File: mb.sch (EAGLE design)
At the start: 32 parts, among them J1 PJ-002BH-SMT-TR, J2 MOLEX_70543-0003MOLEX_70543-0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, J3 MOLEX_70543-0003MOLEX_70543-0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, J4 MOLEX_70543-0003MOLEX_70543-0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, J5 MOLEX_70543-0003MOLEX_70543-0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, Q1 TN0702N3-G, Q2 TN0702N3-G, Q3 TN0702N3-G, Q4 TN0702N3-G, U1 PEM1-S12-S5-S

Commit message: Finalized v1.0 prototype
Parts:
- added R12: 270, ref_lib:YAGEO-CFR-25
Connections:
- net +3.3V: no longer R10.2
- net +5V: now also R12.2
- net GND: now also R10.2, R12.1
- net WP: now also A1.A6
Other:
- moved on the sheet: R10
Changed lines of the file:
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@@
 <class number="0" name="default" width="0" drill="0">
+</class>
+<class number="1" name="POWER" width="1.524" drill="0">
 </class>
 </classes>
@@
 <part name="C3" library="860020672008_Eagle_WCAP-ATG5_rev20a" deviceset="WCAP-ATG5_5X11" device="" package3d_urn="urn:adsk.eagle:package:18308011/2" technology="_860020672001" value="0.1  µF "/>
 <part name="JP5" library="pinhead" library_urn="urn:adsk.eagle:library:325" deviceset="PINHD-1X2" device="" package3d_urn="urn:adsk.eagle:package:22435/2"/>
+<part name="R12" library="ref_lib" deviceset="YAGEO-CFR-25" device="" value="270"/>
 </parts>
 <sheets>
@@
 <attribute name="VALUE" x="-6.858" y="67.31" size="1.778" layer="96" rot="R90"/>
 </instance>
-<instance part="R10" gate="G$1" x="-17.78" y="71.12" smashed="yes" rot="R90">
-<attribute name="NAME" x="-19.2786" y="67.31" size="1.778" layer="95" rot="R90"/>
-<attribute name="VALUE" x="-14.478" y="67.31" size="1.778" layer="96" rot="R90"/>
+<instance part="R10" gate="G$1" x="-17.78" y="50.8" smashed="yes" rot="R270">
+<attribute name="NAME" x="-16.2814" y="54.61" size="1.778" layer="95" rot="R270"/>
+<attribute name="VALUE" x="-21.082" y="54.61" size="1.778" layer="96" rot="R270"/>
 </instance>
 <instance part="R11" gate="G$1" x="30.48" y="71.12" smashed="yes" rot="R90">
@@
 </busses>
 <nets>
-<net name="+12V" class="0">
+<net name="+12V" class="1">
 <segment>
 <pinref part="A1" gate="G$1" pin="VIN"/>
@@
 <pinref part="C3" gate="G$1" pin="-"/>
 <wire x1="-27.94" y1="66.04" x2="-27.94" y2="38.1" width="0.1524" layer="91"/>
-<wire x1="-27.94" y1="38.1" x2="-2.54" y2="38.1" width="0.1524" layer="91"/>
+<wire x1="-27.94" y1="38.1" x2="-17.78" y2="38.1" width="0.1524" layer="91"/>
 <junction x="-2.54" y="38.1"/>
+<pinref part="R10" gate="G$1" pin="2"/>
+<wire x1="-17.78" y1="38.1" x2="-2.54" y2="38.1" width="0.1524" layer="91"/>
+<wire x1="-17.78" y1="45.72" x2="-17.78" y2="38.1" width="0.1524" layer="91"/>
+<junction x="-17.78" y="38.1"/>
 </segment>
 </net>
@@
 <pinref part="R10" gate="G$1" pin="1"/>
 <pinref part="U$1" gate="G$1" pin="WP"/>
-<wire x1="-17.78" y1="66.04" x2="-17.78" y2="58.42" width="0.1524" layer="91"/>
+<wire x1="-17.78" y1="55.88" x2="-17.78" y2="58.42" width="0.1524" layer="91"/>
 <wire x1="-17.78" y1="58.42" x2="-2.54" y2="58.42" width="0.1524" layer="91"/>
 <label x="-17.78" y="58.42" size="1.778" layer="95"/>
+</segment>
+<segment>
+<pinref part="A1" gate="G$1" pin="A6"/>
+<wire x1="55.88" y1="38.1" x2="38.1" y2="38.1" width="0.1524" layer="91"/>
+<label x="38.1" y="38.1" size="1.778" layer="95"/>
 </segment>
 </net>
@@
 <pinref part="R9" gate="G$1" pin="2"/>
 <wire x1="-10.16" y1="76.2" x2="17.78" y2="76.2" width="0.1524" layer="91"/>
-<pinref part="R10" gate="G$1" pin="2"/>
-<wire x1="-17.78" y1="76.2" x2="-10.16" y2="76.2" width="0.1524" layer="91"/>
-<junction x="-10.16" y="76.2"/>
-<pinref part="C3" gate="G$1" pin="+"/>
-<wire x1="-27.94" y1="73.66" x2="-27.94" y2="76.2" width="0.1524" layer="91"/>
-<wire x1="-27.94" y1="76.2" x2="-17.78" y2="76.2" width="0.1524" layer="91"/>
-<junction x="-17.78" y="76.2"/>
 <label x="5.08" y="76.2" size="1.778" layer="95"/>
 <pinref part="A1" gate="G$1" pin="+3V3"/>
 <wire x1="55.88" y1="78.74" x2="17.78" y2="78.74" width="0.1524" layer="91"/>
+<pinref part="C3" gate="G$1" pin="+"/>
+<wire x1="-27.94" y1="73.66" x2="-27.94" y2="76.2" width="0.1524" layer="91"/>
+<wire x1="-10.16" y1="76.2" x2="-27.94" y2="76.2" width="0.1524" layer="91"/>
+<junction x="-10.16" y="76.2"/>
 </segment>
 </net>
@@
 <attribute name="VALUE" x="129.535" y="51.715" size="1.4224" layer="96" rot="R90" align="bottom-center"/>
 </instance>
+<instance part="R12" gate="G$1" x="149.86" y="53.34" smashed="yes" rot="R90">
+<attribute name="NAME" x="148.3614" y="49.53" size="1.778" layer="95" rot="R90"/>
+<attribute name="VALUE" x="153.162" y="49.53" size="1.778" layer="96" rot="R90"/>
+</instance>
 </instances>
 <busses>
@@
 <pinref part="C2" gate="G$1" pin="-"/>
 <wire x1="114.3" y1="48.26" x2="124.46" y2="48.26" width="0.1524" layer="91"/>
-<wire x1="124.46" y1="48.26" x2="144.78" y2="48.26" width="0.1524" layer="91"/>
+<wire x1="124.46" y1="48.26" x2="149.86" y2="48.26" width="0.1524" layer="91"/>
 <junction x="124.46" y="48.26"/>
-<label x="139.7" y="48.26" size="1.778" layer="95"/>
+<label x="154.94" y="48.26" size="1.778" layer="95"/>
+<pinref part="R12" gate="G$1" pin="1"/>
+<wire x1="149.86" y1="48.26" x2="160.02" y2="48.26" width="0.1524" layer="91"/>
+<junction x="149.86" y="48.26"/>
 </segment>
 </net>
@@
 </segment>
 </net>
-<net name="+12V" class="0">
+<net name="+12V" class="1">
 <segment>
 <pinref part="L1" gate="A" pin="2"/>
@@
 <segment>
 <pinref part="U1" gate="G$1" pin="+VO"/>
-<wire x1="114.3" y1="53.34" x2="114.3" y2="55.88" width="0.1524" layer="91"/>
+<wire x1="114.3" y1="53.34" x2="114.3" y2="58.42" width="0.1524" layer="91"/>
+<pinref part="R12" gate="G$1" pin="2"/>
+<wire x1="114.3" y1="58.42" x2="124.46" y2="58.42" width="0.1524" layer="91"/>
 <pinref part="C2" gate="G$1" pin="+"/>
-<wire x1="114.3" y1="55.88" x2="124.46" y2="55.88" width="0.1524" layer="91"/>
-<wire x1="124.46" y1="55.88" x2="144.78" y2="55.88" width="0.1524" layer="91"/>
-<junction x="124.46" y="55.88"/>
-<label x="139.7" y="55.88" size="1.778" layer="95"/>
+<wire x1="124.46" y1="58.42" x2="149.86" y2="58.42" width="0.1524" layer="91"/>
+<wire x1="124.46" y1="55.88" x2="124.46" y2="58.42" width="0.1524" layer="91"/>
+<junction x="124.46" y="58.42"/>
+<label x="154.94" y="58.42" size="1.778" layer="95"/>
+<wire x1="149.86" y1="58.42" x2="160.02" y2="58.42" width="0.1524" layer="91"/>
+<junction x="149.86" y="58.42"/>
 </segment>
 </net>
@@
 </segment>
 </net>
-<net name="+12V" class="0">
+<net name="+12V" class="1">
 <segment>
 <pinref part="J2" gate="G$0" pin="4"/>

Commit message: First built boards
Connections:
- net +3.3V: now also R10.2
- net GND: no longer R10.2
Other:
- moved on the sheet: R10
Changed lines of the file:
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@@
 <attribute name="VALUE" x="-6.858" y="67.31" size="1.778" layer="96" rot="R90"/>
 </instance>
-<instance part="R10" gate="G$1" x="-17.78" y="50.8" smashed="yes" rot="R270">
-<attribute name="NAME" x="-16.2814" y="54.61" size="1.778" layer="95" rot="R270"/>
-<attribute name="VALUE" x="-21.082" y="54.61" size="1.778" layer="96" rot="R270"/>
+<instance part="R10" gate="G$1" x="-17.78" y="71.12" smashed="yes" rot="R90">
+<attribute name="NAME" x="-19.2786" y="67.31" size="1.778" layer="95" rot="R90"/>
+<attribute name="VALUE" x="-14.478" y="67.31" size="1.778" layer="96" rot="R90"/>
 </instance>
 <instance part="R11" gate="G$1" x="30.48" y="71.12" smashed="yes" rot="R90">
@@
 <pinref part="C3" gate="G$1" pin="-"/>
 <wire x1="-27.94" y1="66.04" x2="-27.94" y2="38.1" width="0.1524" layer="91"/>
-<wire x1="-27.94" y1="38.1" x2="-17.78" y2="38.1" width="0.1524" layer="91"/>
 <junction x="-2.54" y="38.1"/>
-<pinref part="R10" gate="G$1" pin="2"/>
-<wire x1="-17.78" y1="38.1" x2="-2.54" y2="38.1" width="0.1524" layer="91"/>
-<wire x1="-17.78" y1="45.72" x2="-17.78" y2="38.1" width="0.1524" layer="91"/>
-<junction x="-17.78" y="38.1"/>
+<wire x1="-27.94" y1="38.1" x2="-2.54" y2="38.1" width="0.1524" layer="91"/>
 </segment>
 </net>
@@
 <pinref part="R10" gate="G$1" pin="1"/>
 <pinref part="U$1" gate="G$1" pin="WP"/>
-<wire x1="-17.78" y1="55.88" x2="-17.78" y2="58.42" width="0.1524" layer="91"/>
+<wire x1="-17.78" y1="66.04" x2="-17.78" y2="58.42" width="0.1524" layer="91"/>
 <wire x1="-17.78" y1="58.42" x2="-2.54" y2="58.42" width="0.1524" layer="91"/>
 <label x="-17.78" y="58.42" size="1.778" layer="95"/>
@@
 <pinref part="C3" gate="G$1" pin="+"/>
 <wire x1="-27.94" y1="73.66" x2="-27.94" y2="76.2" width="0.1524" layer="91"/>
-<wire x1="-10.16" y1="76.2" x2="-27.94" y2="76.2" width="0.1524" layer="91"/>
+<wire x1="-10.16" y1="76.2" x2="-17.78" y2="76.2" width="0.1524" layer="91"/>
 <junction x="-10.16" y="76.2"/>
+<pinref part="R10" gate="G$1" pin="2"/>
+<wire x1="-17.78" y1="76.2" x2="-27.94" y2="76.2" width="0.1524" layer="91"/>
+<junction x="-17.78" y="76.2"/>
 </segment>
 </net>

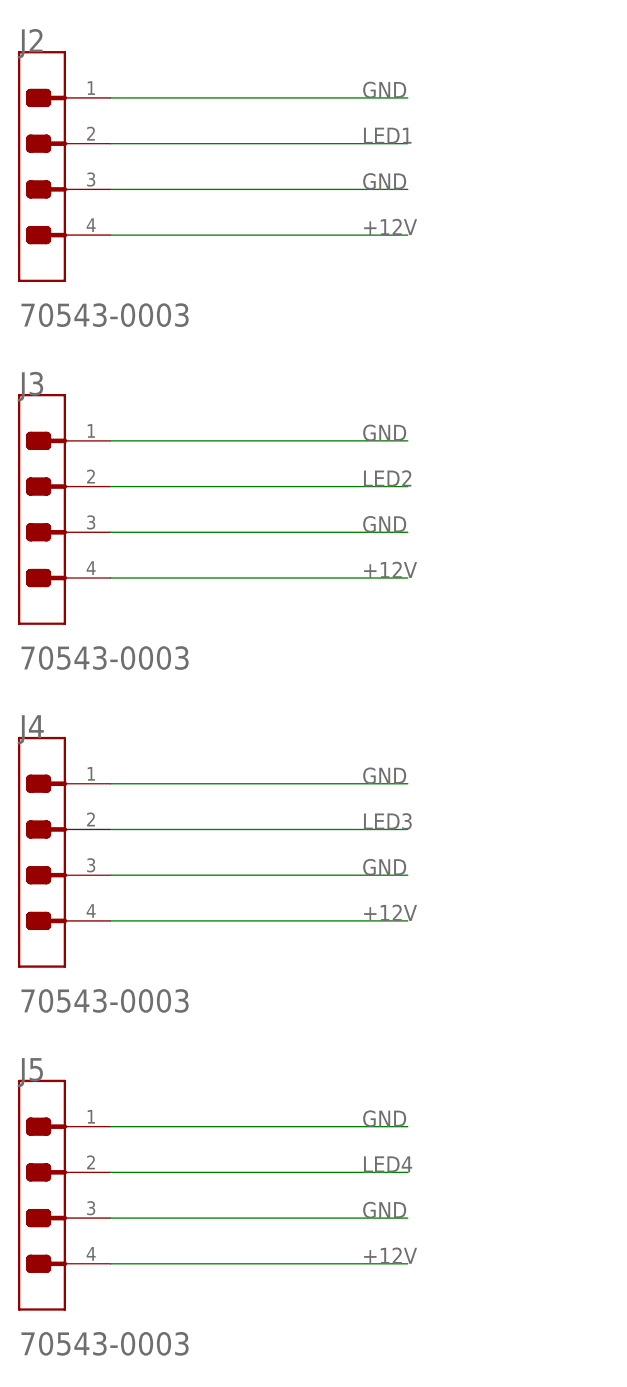
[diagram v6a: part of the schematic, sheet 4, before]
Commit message: Fixing D0 B0 flip
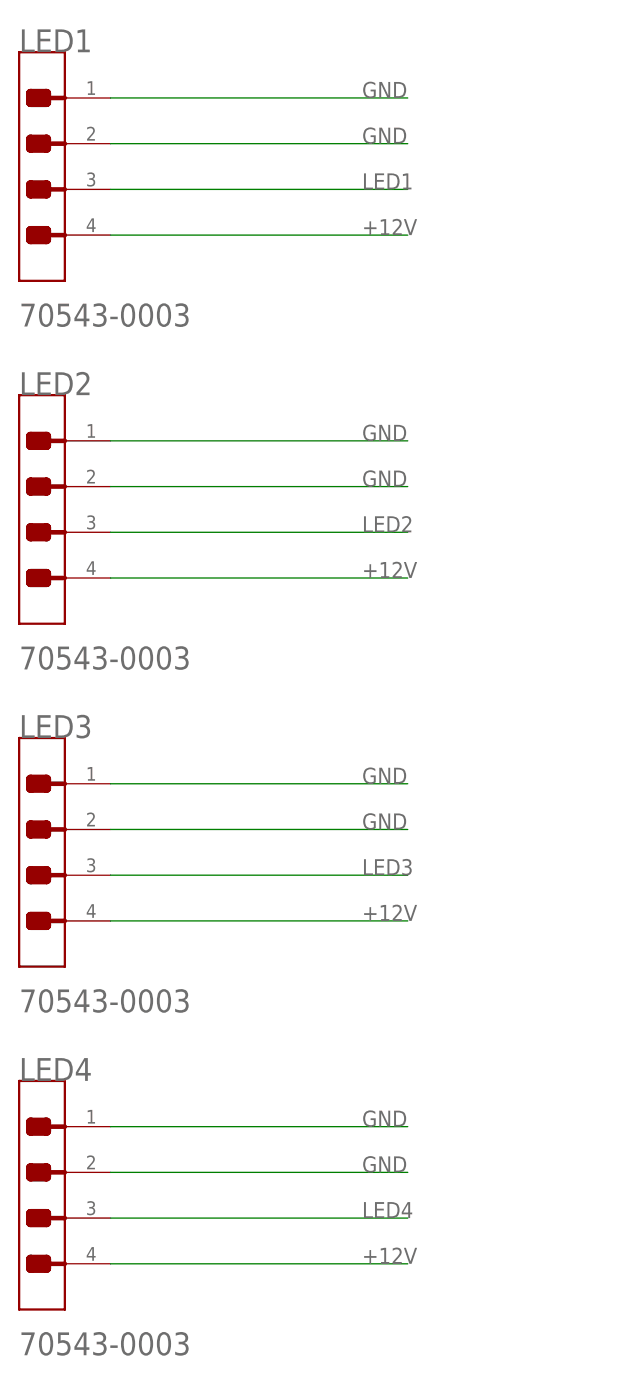
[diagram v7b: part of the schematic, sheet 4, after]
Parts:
- renumbered J2 to LED1, J3 to LED2, J4 to LED3, J5 to LED4
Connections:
- net GND: now also LED1.2, LED2.2, LED3.2, LED4.2; no longer LED1.3, LED2.3, LED3.3, LED4.3
- net LED1: now also LED1.3; no longer LED1.2
- net LED2: now also LED2.3; no longer LED2.2
- net LED3: now also LED3.3; no longer LED3.2
- net LED4: now also LED4.3; no longer LED4.2
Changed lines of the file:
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@@
 <part name="R7" library="ref_lib" deviceset="YAGEO-CFR-25" device="" value="10k"/>
 <part name="R8" library="ref_lib" deviceset="YAGEO-CFR-25" device="" value="10k"/>
-<part name="J2" library="Molex - 70543-0003" deviceset="MOLEX_70543-0003" device="MOLEX_70543-0003_0_0"/>
-<part name="J3" library="Molex - 70543-0003" deviceset="MOLEX_70543-0003" device="MOLEX_70543-0003_0_0"/>
-<part name="J4" library="Molex - 70543-0003" deviceset="MOLEX_70543-0003" device="MOLEX_70543-0003_0_0"/>
-<part name="J5" library="Molex - 70543-0003" deviceset="MOLEX_70543-0003" device="MOLEX_70543-0003_0_0"/>
+<part name="LED1" library="Molex - 70543-0003" deviceset="MOLEX_70543-0003" device="MOLEX_70543-0003_0_0"/>
+<part name="LED2" library="Molex - 70543-0003" deviceset="MOLEX_70543-0003" device="MOLEX_70543-0003_0_0"/>
+<part name="LED3" library="Molex - 70543-0003" deviceset="MOLEX_70543-0003" device="MOLEX_70543-0003_0_0"/>
+<part name="LED4" library="Molex - 70543-0003" deviceset="MOLEX_70543-0003" device="MOLEX_70543-0003_0_0"/>
 <part name="JP1" library="pinhead" library_urn="urn:adsk.eagle:library:325" deviceset="PINHD-1X3" device="/90" package3d_urn="urn:adsk.eagle:package:22459/2"/>
 <part name="JP2" library="pinhead" library_urn="urn:adsk.eagle:library:325" deviceset="PINHD-1X3" device="/90" package3d_urn="urn:adsk.eagle:package:22459/2"/>
@@
 </plain>
 <instances>
-<instance part="J2" gate="G$0" x="10.16" y="147.32" smashed="yes">
+<instance part="LED1" gate="G$0" x="10.16" y="147.32" smashed="yes">
 <attribute name="NAME" x="12.7" y="144.78" size="2.54" layer="95" align="top-left"/>
 </instance>
-<instance part="J3" gate="G$0" x="10.16" y="109.22" smashed="yes">
+<instance part="LED2" gate="G$0" x="10.16" y="109.22" smashed="yes">
 <attribute name="NAME" x="12.7" y="106.68" size="2.54" layer="95" align="top-left"/>
 </instance>
-<instance part="J4" gate="G$0" x="10.16" y="71.12" smashed="yes">
+<instance part="LED3" gate="G$0" x="10.16" y="71.12" smashed="yes">
 <attribute name="NAME" x="12.7" y="68.58" size="2.54" layer="95" align="top-left"/>
 </instance>
-<instance part="J5" gate="G$0" x="10.16" y="33.02" smashed="yes">
+<instance part="LED4" gate="G$0" x="10.16" y="33.02" smashed="yes">
 <attribute name="NAME" x="12.7" y="30.48" size="2.54" layer="95" align="top-left"/>
 </instance>
@@
 <net name="GND" class="0">
 <segment>
-<pinref part="J2" gate="G$0" pin="1"/>
+<pinref part="LED1" gate="G$0" pin="1"/>
 <wire x1="22.86" y1="137.16" x2="55.88" y2="137.16" width="0.1524" layer="91"/>
 <label x="50.8" y="137.16" size="1.778" layer="95"/>
 </segment>
 <segment>
-<pinref part="J2" gate="G$0" pin="3"/>
-<wire x1="22.86" y1="127" x2="55.88" y2="127" width="0.1524" layer="91"/>
-<label x="50.8" y="127" size="1.778" layer="95"/>
-</segment>
-<segment>
-<pinref part="J3" gate="G$0" pin="1"/>
+<pinref part="LED2" gate="G$0" pin="1"/>
 <wire x1="22.86" y1="99.06" x2="55.88" y2="99.06" width="0.1524" layer="91"/>
 <label x="50.8" y="99.06" size="1.778" layer="95"/>
 </segment>
 <segment>
-<pinref part="J3" gate="G$0" pin="3"/>
-<wire x1="22.86" y1="88.9" x2="55.88" y2="88.9" width="0.1524" layer="91"/>
-<label x="50.8" y="88.9" size="1.778" layer="95"/>
-</segment>
-<segment>
-<pinref part="J4" gate="G$0" pin="1"/>
+<pinref part="LED3" gate="G$0" pin="1"/>
 <wire x1="22.86" y1="60.96" x2="55.88" y2="60.96" width="0.1524" layer="91"/>
 <label x="50.8" y="60.96" size="1.778" layer="95"/>
 </segment>
 <segment>
-<pinref part="J4" gate="G$0" pin="3"/>
-<wire x1="22.86" y1="50.8" x2="55.88" y2="50.8" width="0.1524" layer="91"/>
-<label x="50.8" y="50.8" size="1.778" layer="95"/>
-</segment>
-<segment>
-<pinref part="J5" gate="G$0" pin="1"/>
+<pinref part="LED4" gate="G$0" pin="1"/>
 <wire x1="22.86" y1="22.86" x2="55.88" y2="22.86" width="0.1524" layer="91"/>
 <label x="50.8" y="22.86" size="1.778" layer="95"/>
-</segment>
-<segment>
-<pinref part="J5" gate="G$0" pin="3"/>
-<wire x1="22.86" y1="12.7" x2="55.88" y2="12.7" width="0.1524" layer="91"/>
-<label x="50.8" y="12.7" size="1.778" layer="95"/>
 </segment>
 <segment>
@@
 <label x="124.46" y="12.7" size="1.778" layer="95"/>
 </segment>
+<segment>
+<pinref part="LED2" gate="G$0" pin="2"/>
+<wire x1="22.86" y1="93.98" x2="55.88" y2="93.98" width="0.1524" layer="91"/>
+<label x="50.8" y="93.98" size="1.778" layer="95"/>
+</segment>
+<segment>
+<pinref part="LED1" gate="G$0" pin="2"/>
+<wire x1="22.86" y1="132.08" x2="55.88" y2="132.08" width="0.1524" layer="91"/>
+<label x="50.8" y="132.08" size="1.778" layer="95"/>
+</segment>
+<segment>
+<pinref part="LED3" gate="G$0" pin="2"/>
+<wire x1="22.86" y1="55.88" x2="55.88" y2="55.88" width="0.1524" layer="91"/>
+<label x="50.8" y="55.88" size="1.778" layer="95"/>
+</segment>
+<segment>
+<pinref part="LED4" gate="G$0" pin="2"/>
+<wire x1="22.86" y1="17.78" x2="55.88" y2="17.78" width="0.1524" layer="91"/>
+<label x="50.8" y="17.78" size="1.778" layer="95"/>
+</segment>
 </net>
 <net name="+12V" class="1">
 <segment>
-<pinref part="J2" gate="G$0" pin="4"/>
+<pinref part="LED1" gate="G$0" pin="4"/>
 <wire x1="22.86" y1="121.92" x2="55.88" y2="121.92" width="0.1524" layer="91"/>
 <label x="50.8" y="121.92" size="1.778" layer="95"/>
 </segment>
 <segment>
-<pinref part="J3" gate="G$0" pin="4"/>
+<pinref part="LED2" gate="G$0" pin="4"/>
 <wire x1="22.86" y1="83.82" x2="55.88" y2="83.82" width="0.1524" layer="91"/>
 <label x="50.8" y="83.82" size="1.778" layer="95"/>
 </segment>
 <segment>
-<pinref part="J4" gate="G$0" pin="4"/>
+<pinref part="LED3" gate="G$0" pin="4"/>
 <wire x1="22.86" y1="45.72" x2="55.88" y2="45.72" width="0.1524" layer="91"/>
 <label x="50.8" y="45.72" size="1.778" layer="95"/>
 </segment>
 <segment>
-<pinref part="J5" gate="G$0" pin="4"/>
+<pinref part="LED4" gate="G$0" pin="4"/>
 <wire x1="22.86" y1="7.62" x2="55.88" y2="7.62" width="0.1524" layer="91"/>
 <label x="50.8" y="7.62" size="1.778" layer="95"/>
@@
 <net name="LED1" class="0">
 <segment>
-<pinref part="J2" gate="G$0" pin="2"/>
-<wire x1="22.86" y1="132.08" x2="55.88" y2="132.08" width="0.1524" layer="91"/>
-<label x="50.8" y="132.08" size="1.778" layer="95"/>
-</segment>
-</net>
-<net name="LED2" class="0">
-<segment>
-<pinref part="J3" gate="G$0" pin="2"/>
-<wire x1="22.86" y1="93.98" x2="55.88" y2="93.98" width="0.1524" layer="91"/>
-<label x="50.8" y="93.98" size="1.778" layer="95"/>
-</segment>
-</net>
-<net name="LED3" class="0">
-<segment>
-<pinref part="J4" gate="G$0" pin="2"/>
-<wire x1="22.86" y1="55.88" x2="55.88" y2="55.88" width="0.1524" layer="91"/>
-<label x="50.8" y="55.88" size="1.778" layer="95"/>
+<pinref part="LED1" gate="G$0" pin="3"/>
+<wire x1="22.86" y1="127" x2="55.88" y2="127" width="0.1524" layer="91"/>
+<label x="50.8" y="127" size="1.778" layer="95"/>
 </segment>
 </net>
 <net name="LED4" class="0">
 <segment>
-<pinref part="J5" gate="G$0" pin="2"/>
-<wire x1="22.86" y1="17.78" x2="55.88" y2="17.78" width="0.1524" layer="91"/>
-<label x="50.8" y="17.78" size="1.778" layer="95"/>
+<pinref part="LED4" gate="G$0" pin="3"/>
+<wire x1="22.86" y1="12.7" x2="55.88" y2="12.7" width="0.1524" layer="91"/>
+<label x="50.8" y="12.7" size="1.778" layer="95"/>
 </segment>
 </net>
@@
 </segment>
 </net>
+<net name="LED2" class="0">
+<segment>
+<pinref part="LED2" gate="G$0" pin="3"/>
+<wire x1="22.86" y1="88.9" x2="55.88" y2="88.9" width="0.1524" layer="91"/>
+<label x="50.8" y="88.9" size="1.778" layer="95"/>
+</segment>
+</net>
+<net name="LED3" class="0">
+<segment>
+<pinref part="LED3" gate="G$0" pin="3"/>
+<wire x1="22.86" y1="50.8" x2="55.88" y2="50.8" width="0.1524" layer="91"/>
+<label x="50.8" y="50.8" size="1.778" layer="95"/>
+</segment>
+</net>
